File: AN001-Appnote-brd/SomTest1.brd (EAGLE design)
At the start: 160 x 186.6 mm, 43 parts, among them U1 MAX17043, U2 BQ24195, U3 XCL223

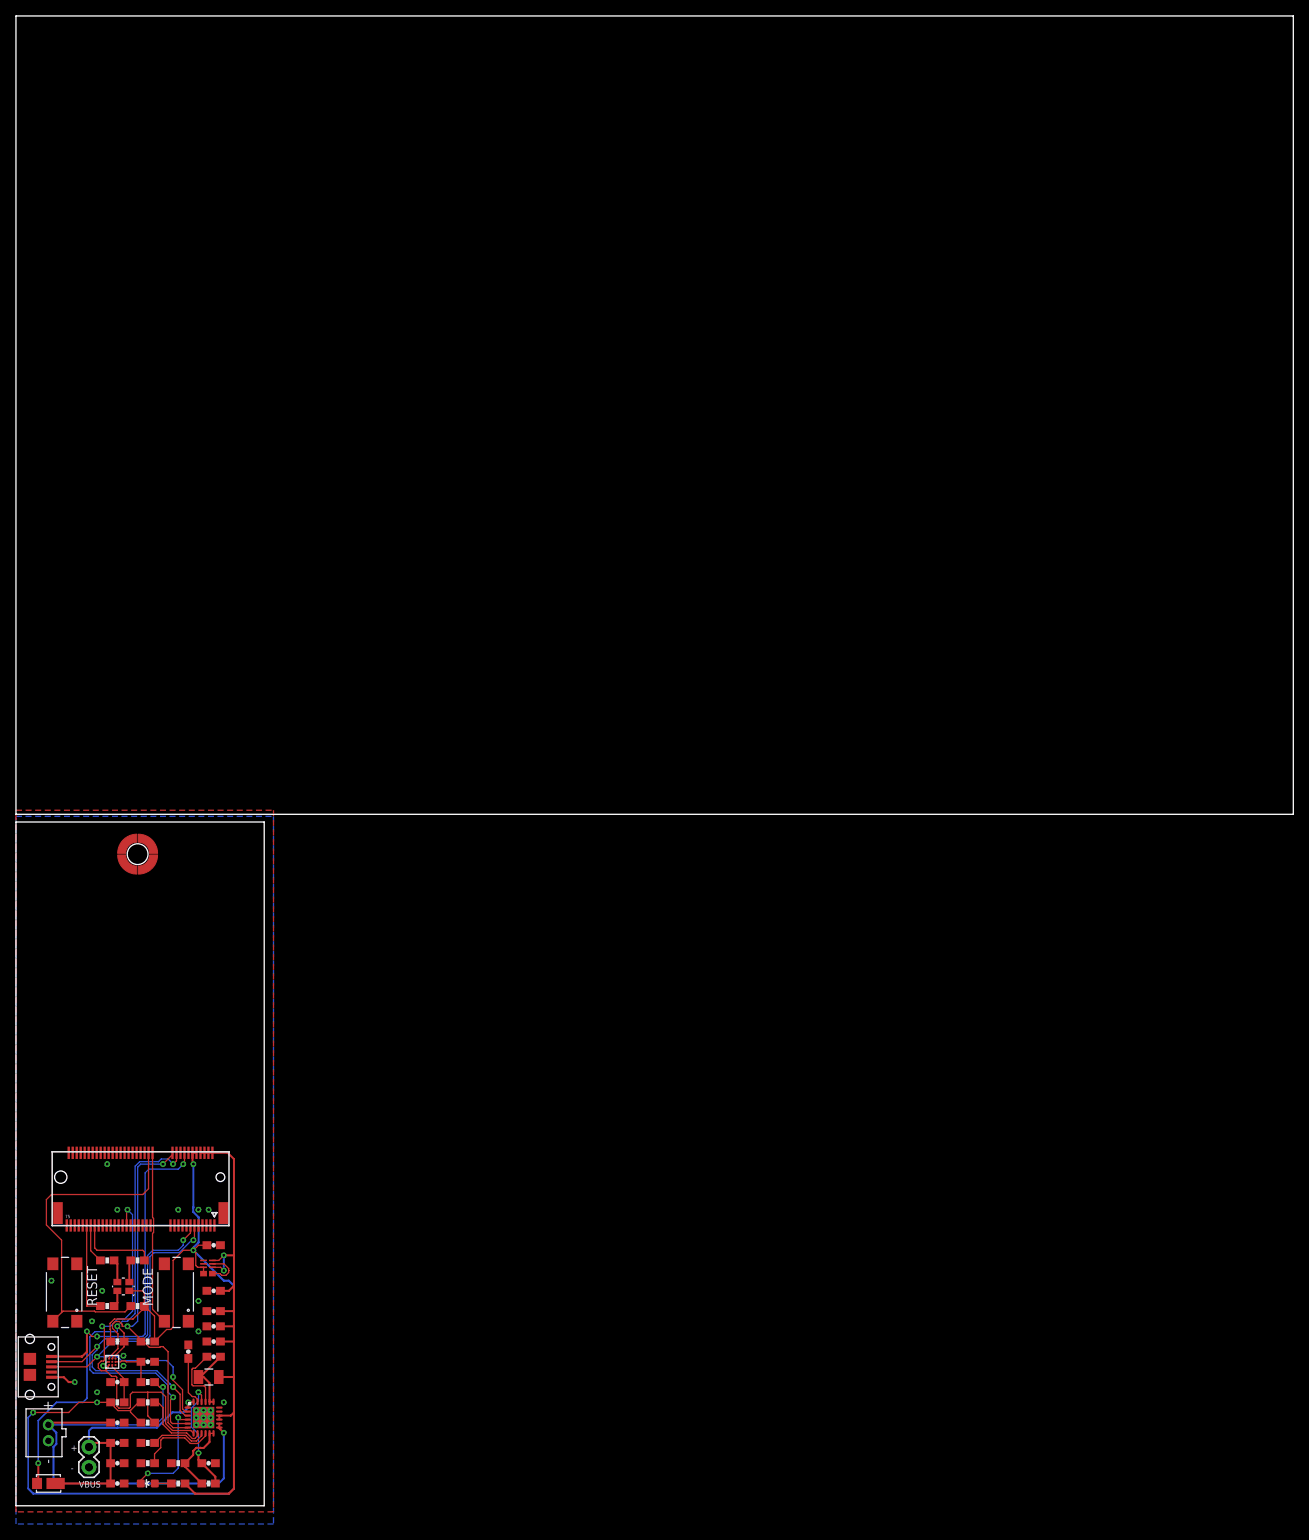
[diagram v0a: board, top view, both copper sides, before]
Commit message: added ricks basic som design as a base
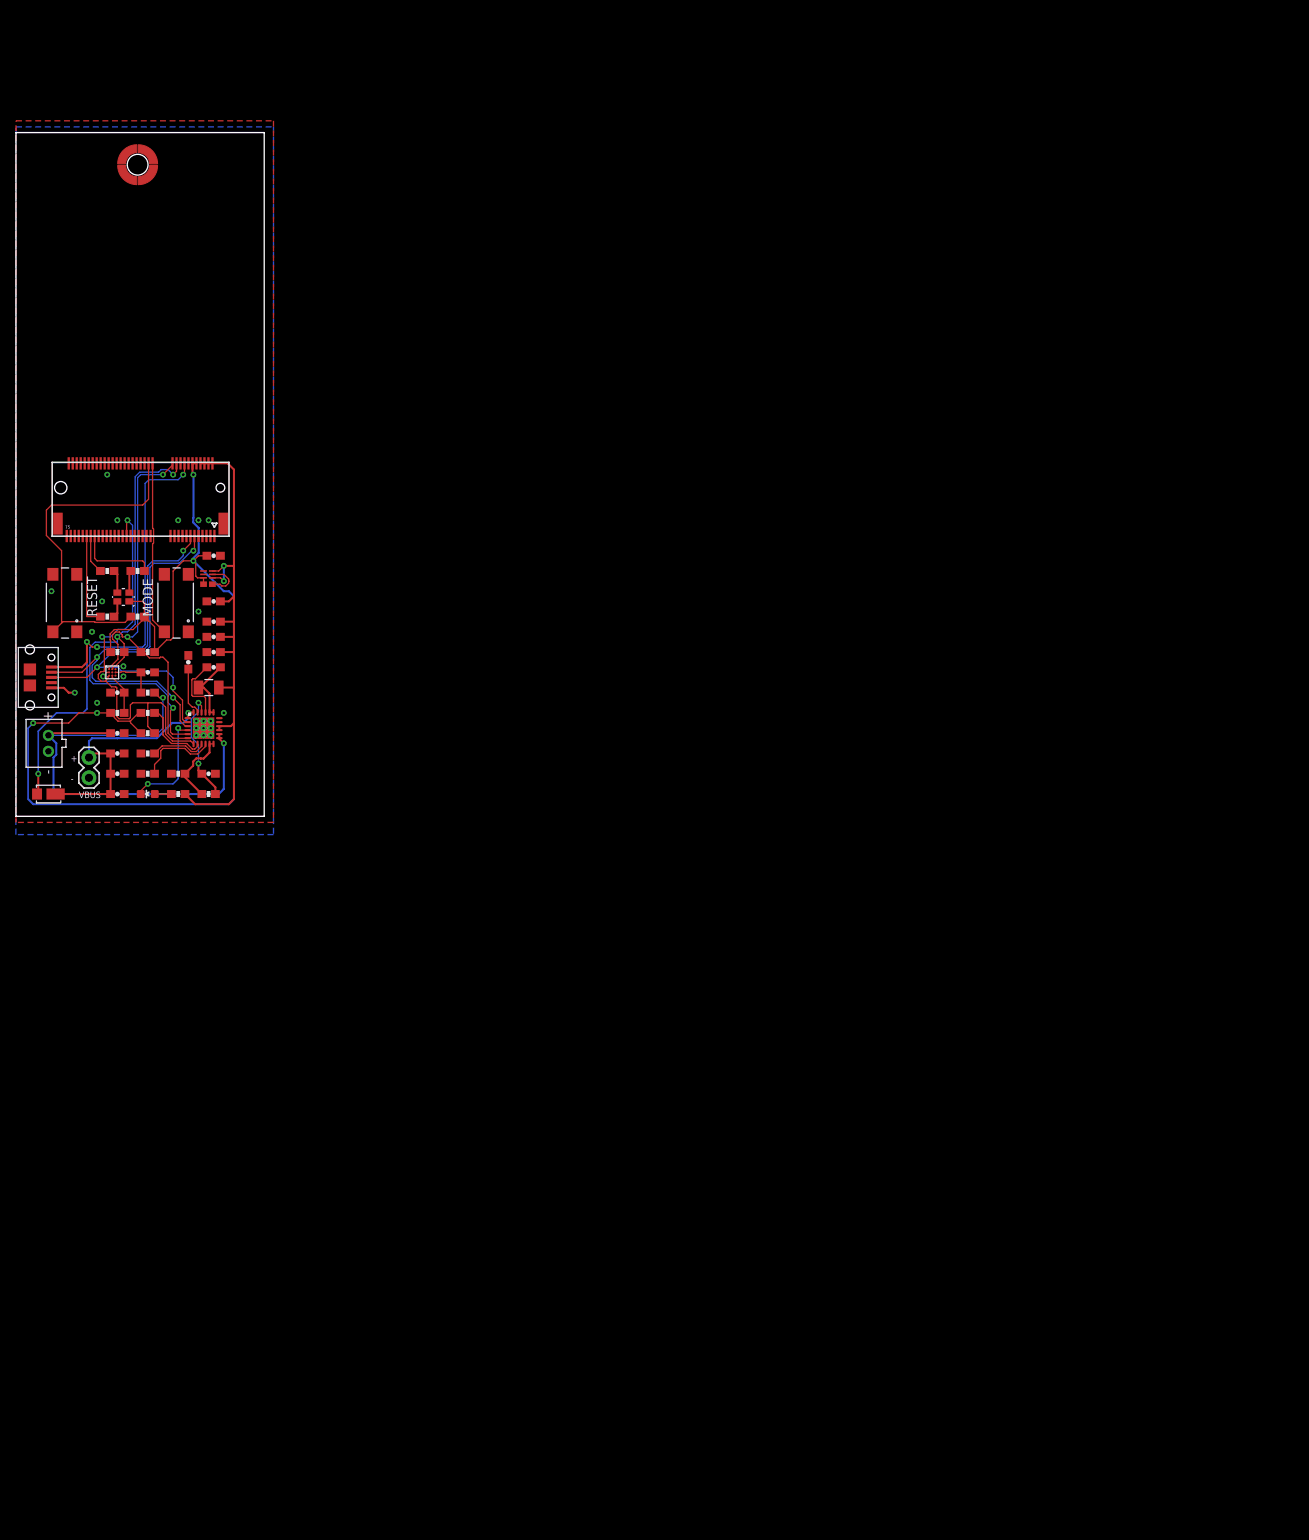
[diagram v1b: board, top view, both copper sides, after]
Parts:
- moved C10 86.4 mm to (24.8, 22.2)
- moved C11 86.4 mm to (24.8, 20.3)
- moved R7 86.4 mm to (16.5, 20.3)
- moved R8 86.4 mm to (12.7, 20.3)
- moved C1 86.4 mm to (12.7, 15.2)
- moved C13 86.4 mm to (24.8, 26.7)
- moved C14 86.4 mm to (24.8, 32.4)
- moved C2 86.4 mm to (12.7, 5.08)
- moved C3 86.4 mm to (16.5, 17.8)
- moved C4 86.4 mm to (21.6, 19.1)
- moved C5 86.4 mm to (12.7, 2.54)
- moved C6 86.4 mm to (12.7, 7.62)
- moved C7 86.4 mm to (12.7, 10.2)
- moved C8 86.4 mm to (24.1, 5.08)
- moved C9 86.4 mm to (24.8, 24.1)
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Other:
- board size 160 x 186.6 mm -> 31.1 x 85.6 mm
